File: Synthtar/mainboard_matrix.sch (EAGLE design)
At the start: 83 parts, among them IC1 74HC164N, IC2 4081N, IC3 555, IC4 4081N, J1 AUDIO_JACK_3.5MM_PTH, M1 ARDUINO-NANO-3.0, U1 JOYSTICKPTH, X1 HD44780LCD-1602, X2 MINI-USB-UX60A-MB-5ST

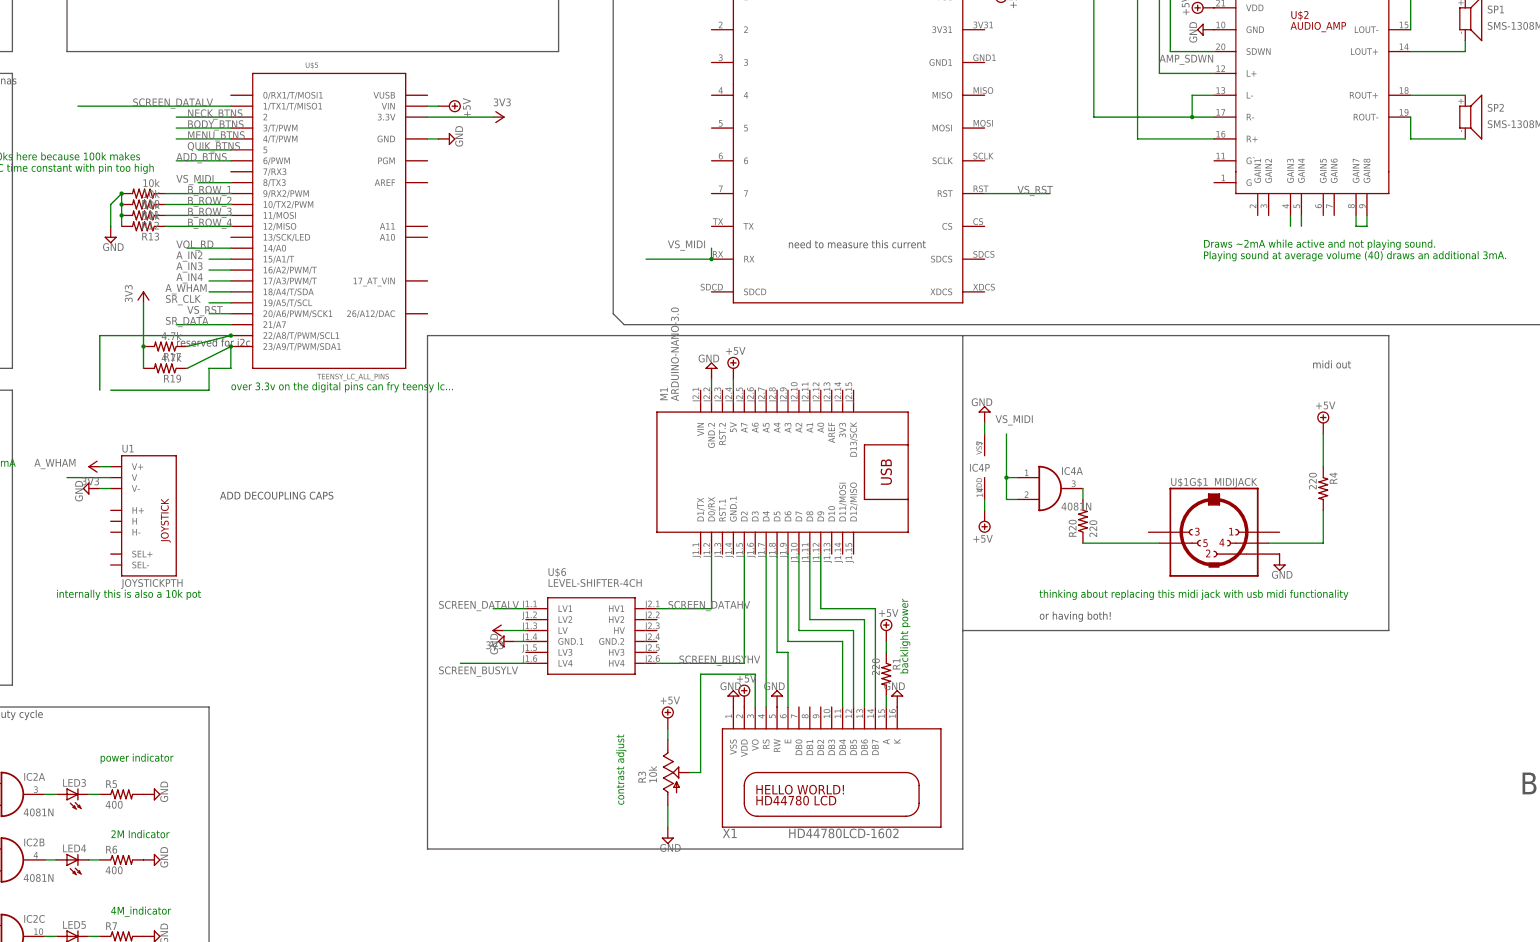
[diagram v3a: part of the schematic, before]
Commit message: midi transmitter + lots of others
midi transmitter board, main motherboard with headers to connect to everything else
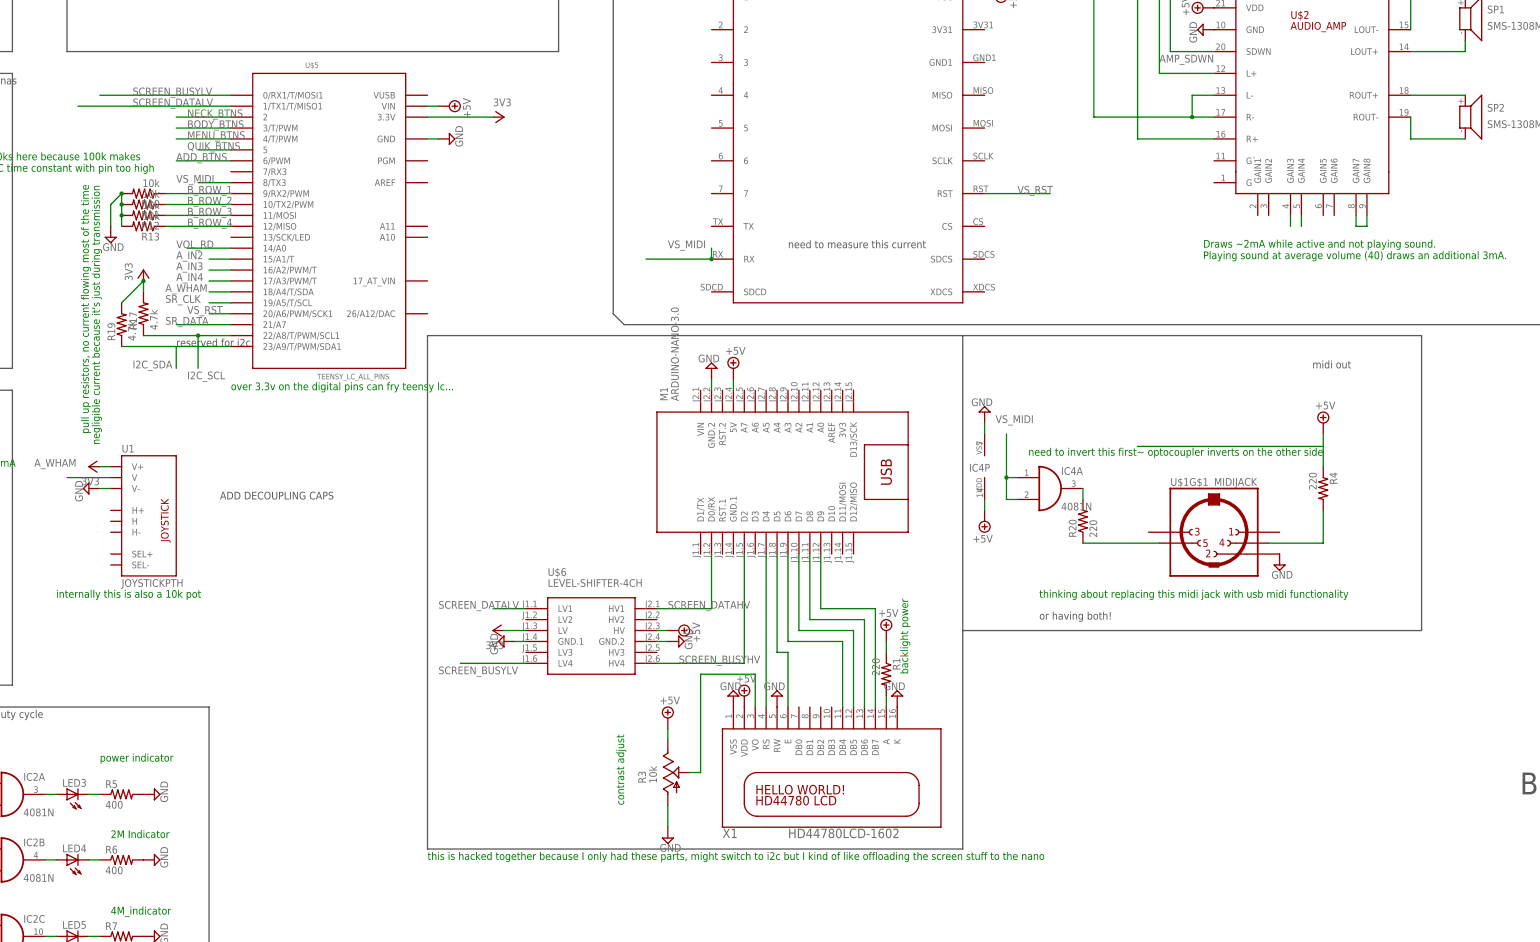
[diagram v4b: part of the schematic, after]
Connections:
- net N$10 renamed I2C_SCL
- net N$8 renamed I2C_SDA
- net +5V: now also U$6.HV
- net GND: now also U$6.GND.2
- net SCREEN_BUSYLV: now also U$5.0/RX1/T/MOSI1
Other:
- note added: "need to invert this first!~ optocoupler inverts on the other side"
- note added: "negligible current because it's just during transmission"
- note added: "pull up resistors, no current flowing most of the time"
- note added: "this is hacked together because I only had these parts, might switch to i2c but I kind of like offloading the screen stuff to the nano"
- moved on the sheet: R17, R19
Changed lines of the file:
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@@
 <part name="P+5" library="supply1" library_urn="urn:adsk.eagle:library:371" deviceset="VCC" device="" value="3V3"/>
 <part name="SUPPLY42" library="supply2" library_urn="urn:adsk.eagle:library:372" deviceset="GND" device=""/>
+<part name="SUPPLY43" library="supply2" library_urn="urn:adsk.eagle:library:372" deviceset="GND" device=""/>
+<part name="SUPPLY44" library="supply2" library_urn="urn:adsk.eagle:library:372" deviceset="+5V" device=""/>
 </parts>
 <sheets>
@@
 <wire x1="-314.96" y1="-2.54" x2="-375.92" y2="-2.54" width="0.1524" layer="97"/>
 <wire x1="-375.92" y1="-2.54" x2="-375.92" y2="66.04" width="0.1524" layer="97"/>
-<wire x1="35.56" y1="78.74" x2="134.62" y2="78.74" width="0.1524" layer="97"/>
-<wire x1="134.62" y1="78.74" x2="134.62" y2="10.16" width="0.1524" layer="97"/>
+<wire x1="35.56" y1="78.74" x2="142.24" y2="78.74" width="0.1524" layer="97"/>
+<wire x1="142.24" y1="78.74" x2="142.24" y2="10.16" width="0.1524" layer="97"/>
 <wire x1="35.56" y1="-40.64" x2="35.56" y2="10.16" width="0.1524" layer="97"/>
 <text x="-345.44" y="63.5" size="1.778" layer="97">voume control</text>
@@
 <text x="-43.18" y="-30.48" size="1.778" layer="91" rot="R90">contrast adjust</text>
 <text x="22.86" y="0" size="1.778" layer="91" rot="R90">backlight power</text>
-<wire x1="134.62" y1="10.16" x2="35.56" y2="10.16" width="0.1524" layer="97"/>
+<wire x1="142.24" y1="10.16" x2="35.56" y2="10.16" width="0.1524" layer="97"/>
 <text x="-370.84" y="60.96" size="1.778" layer="91">lc adc uses 3.3v reference</text>
 <text x="-175.26" y="17.78" size="1.778" layer="91">internally this is also a 10k pot</text>
+<text x="-167.64" y="55.88" size="1.778" layer="91" rot="R90">pull up resistors, no current flowing most of the time</text>
+<text x="-165.1" y="53.34" size="1.778" layer="91" rot="R90">negligible current because it's just during transmission</text>
+<text x="50.8" y="50.8" size="1.778" layer="91">need to invert this first!~ optocoupler inverts on the other side</text>
+<text x="-88.9" y="-43.18" size="1.778" layer="91">this is hacked together because I only had these parts, might switch to i2c but I kind of like offloading the screen stuff to the nano</text>
 </plain>
 <instances>
@@
 <instance part="SUPPLY40" gate="GND" x="-33.02" y="-38.1"/>
 <instance part="SUPPLY41" gate="GND" x="-7.62" y="-5.08" rot="R180"/>
-<instance part="R17" gate="G$1" x="-149.86" y="76.2" rot="R180"/>
-<instance part="R19" gate="G$1" x="-149.86" y="71.12" rot="R180"/>
-<instance part="P+3" gate="VCC" x="-154.94" y="88.9"/>
+<instance part="R17" gate="G$1" x="-154.94" y="83.82" rot="R90"/>
+<instance part="R19" gate="G$1" x="-160.02" y="81.28" rot="R90"/>
+<instance part="P+3" gate="VCC" x="-154.94" y="93.98"/>
 <instance part="C3" gate="G$1" x="-289.56" y="-33.02" rot="R90"/>
 <instance part="U1" gate="G$1" x="-152.4" y="38.1"/>
 <instance part="P+5" gate="VCC" x="-167.64" y="48.26" rot="R90"/>
 <instance part="SUPPLY42" gate="GND" x="-167.64" y="43.18" rot="R270"/>
+<instance part="SUPPLY43" gate="GND" x="-30.48" y="7.62" rot="R90"/>
+<instance part="SUPPLY44" gate="+5V" x="-30.48" y="10.16" rot="R270"/>
 </instances>
 <busses>
@@
 <pinref part="R17" gate="G$1" pin="2"/>
 <pinref part="P+3" gate="VCC" pin="VCC"/>
-<wire x1="-154.94" y1="86.36" x2="-154.94" y2="76.2" width="0.1524" layer="91"/>
 <pinref part="R19" gate="G$1" pin="2"/>
-<wire x1="-154.94" y1="71.12" x2="-154.94" y2="76.2" width="0.1524" layer="91"/>
-<junction x="-154.94" y="76.2"/>
+<wire x1="-160.02" y1="86.36" x2="-154.94" y2="91.44" width="0.1524" layer="91"/>
+<junction x="-154.94" y="91.44"/>
+<wire x1="-154.94" y1="91.44" x2="-154.94" y2="88.9" width="0.1524" layer="91"/>
 </segment>
 <segment>
@@
 <wire x1="-165.1" y1="43.18" x2="-162.56" y2="43.18" width="0.1524" layer="91"/>
 </segment>
+<segment>
+<pinref part="U$6" gate="G$1" pin="GND.2"/>
+<pinref part="SUPPLY43" gate="GND" pin="GND"/>
+<wire x1="-33.02" y1="7.62" x2="-35.56" y2="7.62" width="0.1524" layer="91"/>
+</segment>
 </net>
 <net name="+5V" class="0">
@@
 <pinref part="X1" gate="G$1" pin="VDD"/>
 <pinref part="SUPPLY35" gate="+5V" pin="+5V"/>
+</segment>
+<segment>
+<pinref part="U$6" gate="G$1" pin="HV"/>
+<pinref part="SUPPLY44" gate="+5V" pin="+5V"/>
+<wire x1="-33.02" y1="10.16" x2="-35.56" y2="10.16" width="0.1524" layer="91"/>
 </segment>
 </net>
@@
 <wire x1="81.28" y1="30.48" x2="63.5" y2="30.48" width="0.1524" layer="91"/>
 <pinref part="R20" gate="G$1" pin="1"/>
-</segment>
-</net>
-<net name="N$8" class="0">
-<segment>
-<pinref part="U$5" gate="G$1" pin="23/A9/T/PWM/SDA1"/>
-<wire x1="-144.78" y1="71.12" x2="-134.62" y2="76.2" width="0.1524" layer="91"/>
-<pinref part="R19" gate="G$1" pin="1"/>
-<wire x1="-134.62" y1="76.2" x2="-134.62" y2="71.12" width="0.1524" layer="91"/>
-<wire x1="-134.62" y1="71.12" x2="-139.7" y2="71.12" width="0.1524" layer="91"/>
-<junction x="-134.62" y="76.2"/>
-<wire x1="-139.7" y1="71.12" x2="-139.7" y2="66.04" width="0.1524" layer="91"/>
-<wire x1="-139.7" y1="66.04" x2="-162.56" y2="66.04" width="0.1524" layer="91"/>
 </segment>
 </net>
@@
 <label x="-86.36" y="0" size="1.778" layer="95"/>
 </segment>
-</net>
-<net name="N$10" class="0">
+<segment>
+<pinref part="U$5" gate="G$1" pin="0/RX1/T/MOSI1"/>
+<wire x1="-134.62" y1="134.62" x2="-165.1" y2="134.62" width="0.1524" layer="91"/>
+<label x="-157.48" y="134.62" size="1.778" layer="95"/>
+</segment>
+</net>
+<net name="I2C_SCL" class="0">
 <segment>
 <pinref part="U$5" gate="G$1" pin="22/A8/T/PWM/SCL1"/>
-<wire x1="-134.62" y1="78.74" x2="-144.78" y2="76.2" width="0.1524" layer="91"/>
+<wire x1="-134.62" y1="78.74" x2="-142.24" y2="78.74" width="0.1524" layer="91"/>
 <pinref part="R17" gate="G$1" pin="1"/>
-<junction x="-134.62" y="78.74"/>
-<wire x1="-134.62" y1="78.74" x2="-165.1" y2="78.74" width="0.1524" layer="91"/>
-<wire x1="-165.1" y1="78.74" x2="-165.1" y2="66.04" width="0.1524" layer="91"/>
+<wire x1="-142.24" y1="78.74" x2="-154.94" y2="78.74" width="0.1524" layer="91"/>
+<wire x1="-142.24" y1="78.74" x2="-142.24" y2="71.12" width="0.1524" layer="91"/>
+<junction x="-142.24" y="78.74"/>
+<label x="-144.78" y="68.58" size="1.778" layer="95"/>
 </segment>
 </net>
@@
 </segment>
 </net>
+<net name="I2C_SDA" class="0">
+<segment>
+<pinref part="U$5" gate="G$1" pin="23/A9/T/PWM/SDA1"/>
+<pinref part="R19" gate="G$1" pin="1"/>
+<wire x1="-160.02" y1="76.2" x2="-147.32" y2="76.2" width="0.1524" layer="91"/>
+<wire x1="-147.32" y1="76.2" x2="-134.62" y2="76.2" width="0.1524" layer="91"/>
+<wire x1="-147.32" y1="76.2" x2="-147.32" y2="71.12" width="0.1524" layer="91"/>
+<label x="-157.48" y="71.12" size="1.778" layer="95"/>
+</segment>
+</net>

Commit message: big changes
changed a ton
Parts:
- added S20: (no value), SparkFun-Switches:SWITCH-SPDT-PTH-11.6X4.0MM
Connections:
- new net N$8: S20.O, U$4.VIN-
- net N$15: now also S20.P; no longer U$4.VIN-
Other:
- note added: "make this an spdt and add a header to connect the signal to the screenboard"
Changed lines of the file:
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@@
 <part name="SUPPLY43" library="supply2" library_urn="urn:adsk.eagle:library:372" deviceset="GND" device=""/>
 <part name="SUPPLY44" library="supply2" library_urn="urn:adsk.eagle:library:372" deviceset="+5V" device=""/>
+<part name="S20" library="SparkFun-Switches" library_urn="urn:adsk.eagle:library:535" deviceset="SWITCH-SPDT" device="-PTH-11.6X4.0MM" package3d_urn="urn:adsk.eagle:package:40177/1"/>
 </parts>
 <sheets>
@@
 <text x="50.8" y="50.8" size="1.778" layer="91">need to invert this first!~ optocoupler inverts on the other side</text>
 <text x="-88.9" y="-43.18" size="1.778" layer="91">this is hacked together because I only had these parts, might switch to i2c but I kind of like offloading the screen stuff to the nano</text>
+<text x="111.76" y="175.26" size="1.778" layer="91">make this an spdt and add a header to connect the signal to the screenboard</text>
 </plain>
 <instances>
@@
 <instance part="SUPPLY43" gate="GND" x="-30.48" y="7.62" rot="R90"/>
 <instance part="SUPPLY44" gate="+5V" x="-30.48" y="10.16" rot="R270"/>
+<instance part="S20" gate="1" x="-121.92" y="157.48"/>
 </instances>
 <busses>
@@
 <pinref part="U$3" gate="G$1" pin="LOAD-"/>
 <wire x1="-129.54" y1="162.56" x2="-129.54" y2="157.48" width="0.1524" layer="91"/>
-<wire x1="-129.54" y1="157.48" x2="-111.76" y2="157.48" width="0.1524" layer="91"/>
-<pinref part="U$4" gate="G$1" pin="VIN-"/>
-<wire x1="-111.76" y1="157.48" x2="-111.76" y2="165.1" width="0.1524" layer="91"/>
+<wire x1="-129.54" y1="157.48" x2="-124.46" y2="157.48" width="0.1524" layer="91"/>
+<pinref part="S20" gate="1" pin="P"/>
 </segment>
 </net>
@@
 </segment>
 </net>
+<net name="N$8" class="0">
+<segment>
+<pinref part="U$4" gate="G$1" pin="VIN-"/>
+<pinref part="S20" gate="1" pin="O"/>
+<wire x1="-111.76" y1="160.02" x2="-111.76" y2="165.1" width="0.1524" layer="91"/>
+<wire x1="-116.84" y1="160.02" x2="-111.76" y2="160.02" width="0.1524" layer="91"/>
+</segment>
+</net>
